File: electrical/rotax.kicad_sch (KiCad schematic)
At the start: 23 parts

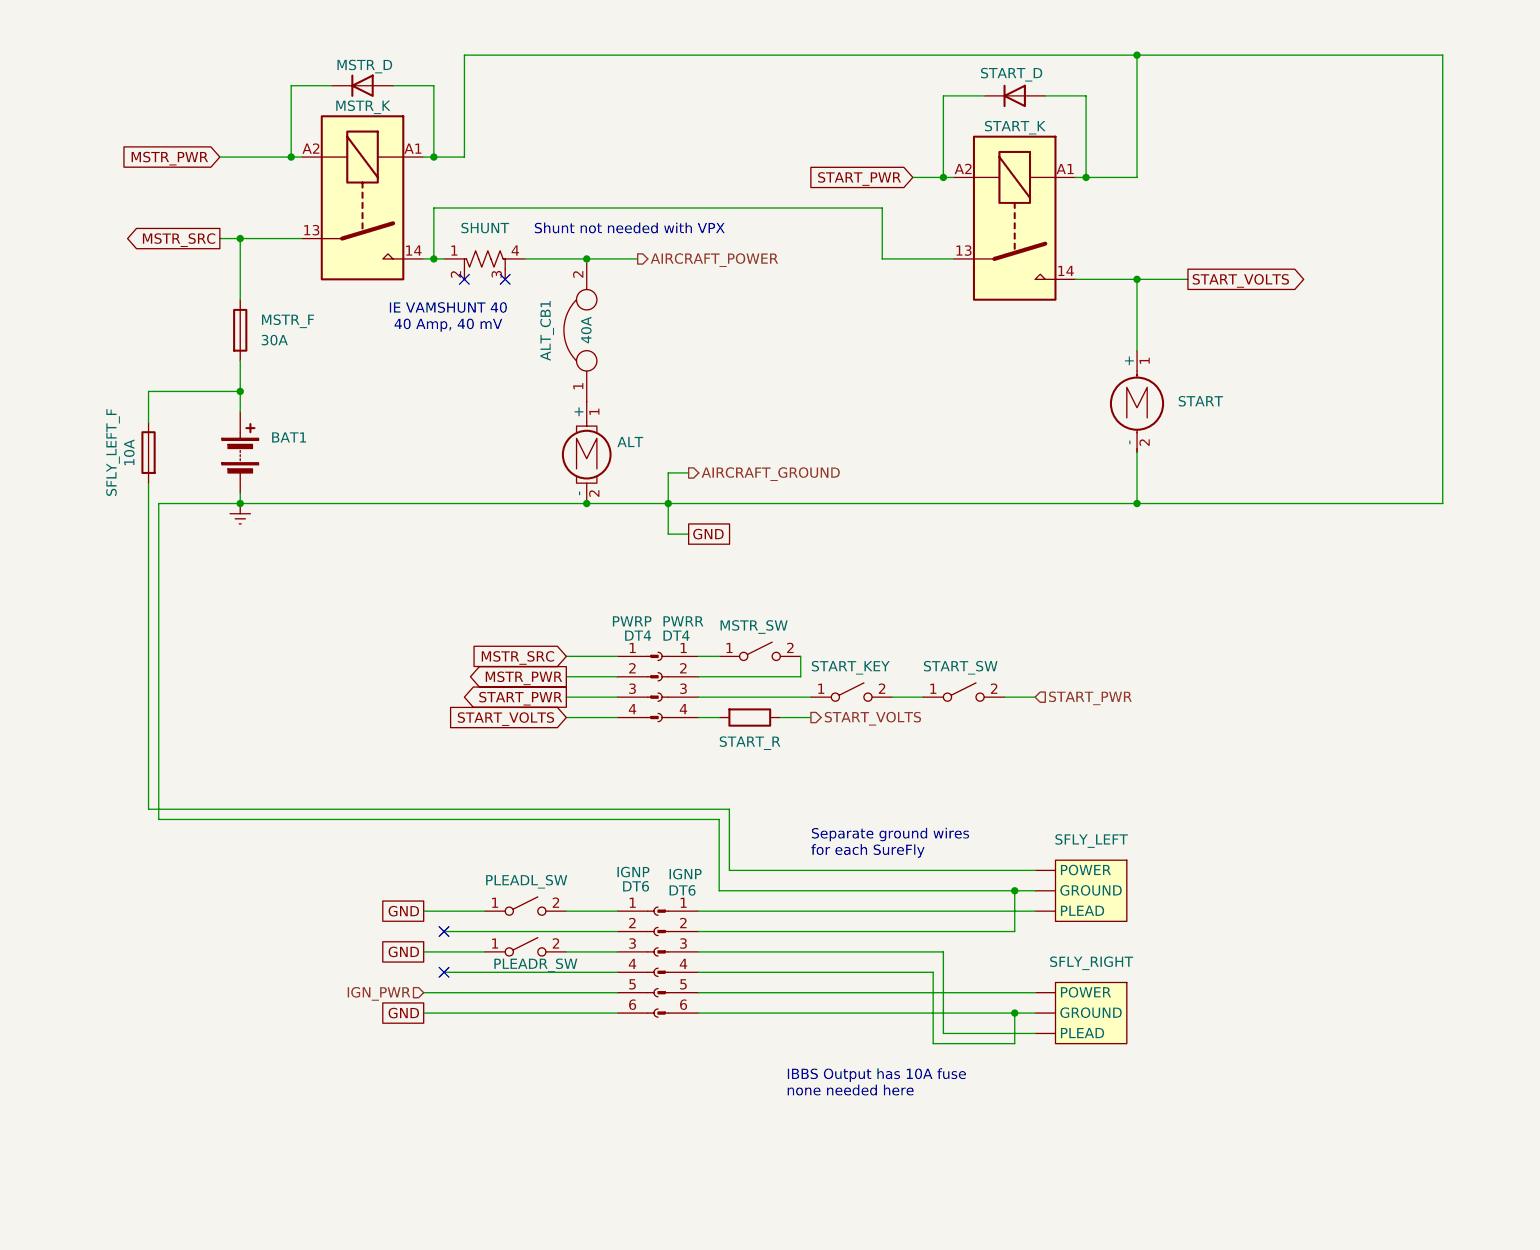
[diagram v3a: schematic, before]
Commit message: Added amperage and gauges for wires.
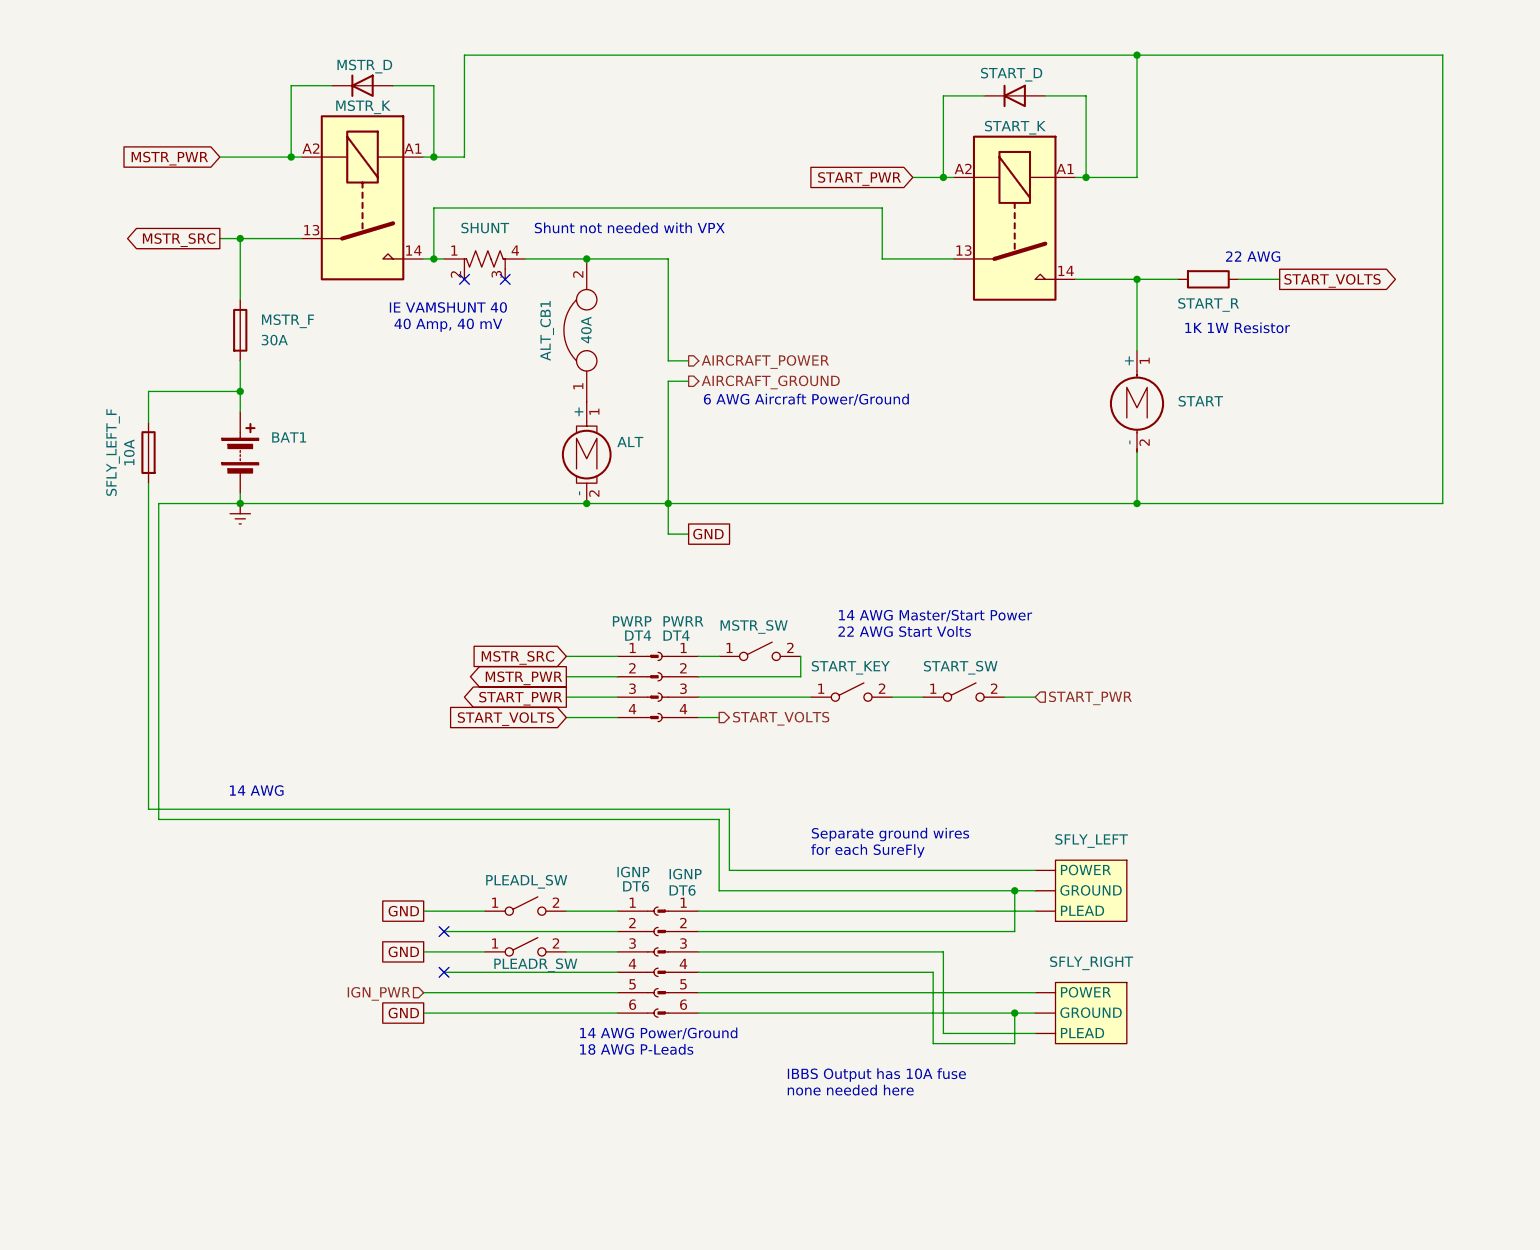
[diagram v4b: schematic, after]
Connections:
- net START_VOLTS: now also PWRR.4 (Pin_4); no longer START.1 (+), START_K.14
- net at START_R.2: now also START.1 (+), START_K.14; no longer PWRR.4 (Pin_4)
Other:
- note added: "14 AWG"
- note added: "14 AWG Master/Start Power 22 AWG Start Volts"
- note added: "14 AWG Power/Ground 18 AWG P-Leads"
- note added: "1K 1W Resistor"
- note added: "22 AWG"
- note added: "6 AWG Aircraft Power/Ground"
- moved on the sheet: START_R
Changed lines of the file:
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@@
 		(title "Lycoming")
 		(date "2025-10-01")
-		(rev "1.1")
+		(rev "1.1.1")
 		(company "N78HR")
 	)
@@
 		)
 	)
+	(text "1K 1W Resistor"
+		(exclude_from_sim no)
+		(at 167.386 53.34 0)
+		(effects
+			(font
+				(size 1.27 1.27)
+			)
+		)
+	)
 	(text "Separate ground wires\nfor each SureFly"
 		(exclude_from_sim no)
@@
 		)
 	)
+	(text "14 AWG Power/Ground\n18 AWG P-Leads"
+		(exclude_from_sim no)
+		(at 85.344 142.24 0)
+		(effects
+			(font
+				(size 1.27 1.27)
+			)
+			(justify left)
+		)
+	)
 	(text "IBBS Output has 10A fuse\nnone needed here"
 		(exclude_from_sim no)
@@
 		)
 	)
+	(text "6 AWG Aircraft Power/Ground"
+		(exclude_from_sim no)
+		(at 100.838 62.23 0)
+		(effects
+			(font
+				(size 1.27 1.27)
+			)
+			(justify left)
+		)
+	)
+	(text "14 AWG Master/Start Power\n22 AWG Start Volts"
+		(exclude_from_sim no)
+		(at 117.602 90.17 0)
+		(effects
+			(font
+				(size 1.27 1.27)
+			)
+			(justify left)
+		)
+	)
 	(text "IE VAMSHUNT 40\n40 Amp, 40 mV"
 		(exclude_from_sim no)
 		(at 69.088 51.816 0)
+		(effects
+			(font
+				(size 1.27 1.27)
+			)
+		)
+	)
+	(text "14 AWG"
+		(exclude_from_sim no)
+		(at 45.212 110.998 0)
+		(effects
+			(font
+				(size 1.27 1.27)
+			)
+		)
+	)
+	(text "22 AWG"
+		(exclude_from_sim no)
+		(at 169.418 44.45 0)
 		(effects
 			(font
@@
 	)
 	(junction
-		(at 154.94 46.99)
-		(diameter 0)
-		(color 0 0 0 0)
-	)
-	(junction
 		(at 96.52 74.93)
 		(diameter 0)
@@
 	)
 	(junction
+		(at 154.94 46.99)
+		(diameter 0)
+		(color 0 0 0 0)
+	)
+	(junction
 		(at 148.59 34.29)
 		(diameter 0)
@@
 	(wire
 		(pts
+			(xy 100.33 101.6) (xy 102.87 101.6)
+		)
+		(stroke
+			(width 0)
+			(type default)
+		)
+	)
+	(wire
+		(pts
 			(xy 100.33 99.06) (xy 114.3 99.06)
 		)
@@
 	(wire
 		(pts
-			(xy 92.71 44.45) (xy 86.36 44.45)
+			(xy 99.06 57.15) (xy 96.52 57.15)
 		)
 		(stroke
@@
 	(wire
 		(pts
-			(xy 100.33 101.6) (xy 102.87 101.6)
-		)
-		(stroke
-			(width 0)
-			(type default)
-		)
-	)
-	(wire
-		(pts
 			(xy 100.33 135.89) (xy 142.24 135.89)
 		)
@@
 	(wire
 		(pts
-			(xy 154.94 46.99) (xy 161.29 46.99)
-		)
-		(stroke
-			(width 0)
-			(type default)
-		)
-	)
-	(wire
-		(pts
 			(xy 68.58 128.27) (xy 90.17 128.27)
 		)
@@
 	(wire
 		(pts
-			(xy 110.49 101.6) (xy 114.3 101.6)
-		)
-		(stroke
-			(width 0)
-			(type default)
-		)
-	)
-	(wire
-		(pts
 			(xy 31.75 72.39) (xy 31.75 113.03)
 		)
@@
 	(wire
 		(pts
+			(xy 96.52 57.15) (xy 96.52 44.45)
+		)
+		(stroke
+			(width 0)
+			(type default)
+		)
+	)
+	(wire
+		(pts
 			(xy 71.12 19.05) (xy 154.94 19.05)
 		)
@@
 	(wire
 		(pts
-			(xy 99.06 71.12) (xy 96.52 71.12)
+			(xy 99.06 59.69) (xy 96.52 59.69)
 		)
 		(stroke
@@
 	(wire
 		(pts
+			(xy 167.64 46.99) (xy 172.72 46.99)
+		)
+		(stroke
+			(width 0)
+			(type default)
+		)
+	)
+	(wire
+		(pts
 			(xy 100.33 138.43) (xy 139.7 138.43)
 		)
@@
 	(wire
 		(pts
+			(xy 154.94 46.99) (xy 160.02 46.99)
+		)
+		(stroke
+			(width 0)
+			(type default)
+		)
+	)
+	(wire
+		(pts
+			(xy 96.52 44.45) (xy 86.36 44.45)
+		)
+		(stroke
+			(width 0)
+			(type default)
+		)
+	)
+	(wire
+		(pts
 			(xy 143.51 24.13) (xy 148.59 24.13)
 		)
@@
 	(wire
 		(pts
-			(xy 96.52 71.12) (xy 96.52 74.93)
+			(xy 96.52 59.69) (xy 96.52 74.93)
 		)
 		(stroke
@@
 	(global_label "START_VOLTS"
 		(shape output)
-		(at 161.29 46.99 0)
+		(at 172.72 46.99 0)
 		(fields_autoplaced yes)
 		(effects
@@
 		)
 		(property "Intersheetrefs" "${INTERSHEET_REFS}"
-			(at 176.3704 46.99 0)
+			(at 187.8004 46.99 0)
 			(effects
 				(font
@@
 	(hierarchical_label "START_VOLTS"
 		(shape output)
-		(at 114.3 101.6 0)
+		(at 102.87 101.6 0)
 		(effects
 			(font
@@
 	(hierarchical_label "AIRCRAFT_POWER"
 		(shape output)
-		(at 92.71 44.45 0)
+		(at 99.06 57.15 0)
 		(effects
 			(font
@@
 	(hierarchical_label "AIRCRAFT_GROUND"
 		(shape output)
-		(at 99.06 71.12 0)
+		(at 99.06 59.69 0)
 		(effects
 			(font
@@
 	(symbol
 		(lib_id "Device:R")
-		(at 106.68 101.6 270)
+		(at 163.83 46.99 270)
 		(unit 1)
 		(exclude_from_sim no)
@@
 		(dnp no)
 		(property "Reference" "START_R"
-			(at 106.68 104.648 90)
+			(at 163.83 50.038 90)
 			(effects
 				(font
@@
 		)
 		(property "Value" "R"
-			(at 105.4101 104.14 0)
+			(at 162.5601 49.53 0)
 			(effects
 				(font
@@
 		)
 		(property "Footprint" ""
-			(at 106.68 99.822 90)
+			(at 163.83 45.212 90)
 			(effects
 				(font
@@
 		)
 		(property "Datasheet" "~"
-			(at 106.68 101.6 0)
+			(at 163.83 46.99 0)
 			(effects
 				(font
@@
 		)
 		(property "Description" "Resistor"
-			(at 106.68 101.6 0)
-			(effects
-				(font
+			(at 163.83 46.99 0)
+			(effects
+				(font

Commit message: Added switch numbers.
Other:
- note added: "RS1"
- note added: "RS2"
- note added: "RS3"
- note added: "RS4"
- note added: "RS5"
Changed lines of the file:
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@@
 	(title_block
 		(title "Lycoming")
-		(date "2025-10-01")
-		(rev "1.1.1")
+		(date "2025-10-02")
+		(rev "1.1.3")
 		(company "N78HR")
 	)
@@
 		)
 	)
+	(text "RS5"
+		(exclude_from_sim no)
+		(at 71.882 124.46 0)
+		(effects
+			(font
+				(size 1.27 1.27)
+			)
+		)
+	)
 	(text "IBBS Output has 10A fuse\nnone needed here"
 		(exclude_from_sim no)
@@
 		)
 	)
+	(text "RS4"
+		(exclude_from_sim no)
+		(at 71.628 132.334 0)
+		(effects
+			(font
+				(size 1.27 1.27)
+			)
+		)
+	)
 	(text "14 AWG Master/Start Power\n22 AWG Start Volts"
 		(exclude_from_sim no)
@@
 			)
 			(justify left)
+		)
+	)
+	(text "RS2"
+		(exclude_from_sim no)
+		(at 133.096 101.854 0)
+		(effects
+			(font
+				(size 1.27 1.27)
+			)
 		)
 	)
@@
 		)
 	)
+	(text "RS3"
+		(exclude_from_sim no)
+		(at 108.204 88.138 0)
+		(effects
+			(font
+				(size 1.27 1.27)
+			)
+		)
+	)
 	(text "22 AWG"
 		(exclude_from_sim no)
@@
 		(effects
 			(font
+				(size 1.27 1.27)
+			)
+		)
+	)
+	(text "RS1"
+		(exclude_from_sim no)
+		(at 121.666 101.6 0)
+		(effects
+			(font

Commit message: Changed wiring of plead connector
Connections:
- net Earth: now also IGNP.4 (Pin_4); no longer IGNP.6 (Pin_6)
- net IGN_PWR: now also IGNP.3 (Pin_3); no longer IGNP.5 (Pin_5)
- net at IGNP.6 (Pin_6), SFLY_RIGHT. (PLEAD): no longer IGNP.4 (Pin_4)
- net at IGNP.5 (Pin_5), SFLY_RIGHT. (PLEAD): now also IGNP.4 (Pin_4)
- net at PLEADR_SW.2 (B): now also IGNP.6 (Pin_6); no longer IGNP.3 (Pin_3)
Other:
- moved on the sheet: PLEADR_SW, SFLY_RIGHT
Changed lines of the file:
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@@
 	(title_block
 		(title "Lycoming")
-		(date "2025-10-02")
-		(rev "1.1.3")
+		(date "2025-10-11")
+		(rev "1.1.7")
 		(company "N78HR")
 	)
@@
 	(text "RS4"
 		(exclude_from_sim no)
-		(at 71.628 132.334 0)
+		(at 71.628 139.954 0)
 		(effects
 			(font
@@
 	)
 	(junction
+		(at 138.43 133.35)
+		(diameter 0)
+		(color 0 0 0 0)
+	)
+	(junction
 		(at 96.52 74.93)
 		(diameter 0)
@@
 	)
 	(junction
-		(at 139.7 138.43)
-		(diameter 0)
-		(color 0 0 0 0)
-	)
-	(junction
 		(at 139.7 123.19)
 		(diameter 0)
@@
 	)
 	(no_connect
-		(at 68.58 133.35)
+		(at 68.58 135.89)
 	)
 	(wire
@@
 	(wire
 		(pts
+			(xy 68.58 135.89) (xy 90.17 135.89)
+		)
+		(stroke
+			(width 0)
+			(type default)
+		)
+	)
+	(wire
+		(pts
 			(xy 100.33 99.06) (xy 114.3 99.06)
 		)
@@
 	(wire
 		(pts
-			(xy 130.81 130.81) (xy 130.81 140.97)
-		)
-		(stroke
-			(width 0)
-			(type default)
-		)
-	)
-	(wire
-		(pts
 			(xy 100.33 93.98) (xy 102.87 93.98)
 		)
@@
 	(wire
 		(pts
-			(xy 66.04 138.43) (xy 90.17 138.43)
+			(xy 140.97 135.89) (xy 140.97 138.43)
 		)
 		(stroke
@@
 	(wire
 		(pts
-			(xy 66.04 130.81) (xy 73.66 130.81)
+			(xy 66.04 138.43) (xy 73.66 138.43)
 		)
 		(stroke
@@
 	(wire
 		(pts
+			(xy 140.97 135.89) (xy 142.24 135.89)
+		)
+		(stroke
+			(width 0)
+			(type default)
+		)
+	)
+	(wire
+		(pts
 			(xy 100.33 125.73) (xy 142.24 125.73)
 		)
@@
 	(wire
 		(pts
-			(xy 100.33 135.89) (xy 142.24 135.89)
-		)
-		(stroke
-			(width 0)
-			(type default)
-		)
-	)
-	(wire
-		(pts
 			(xy 40.64 41.91) (xy 43.18 41.91)
 		)
@@
 	(wire
 		(pts
-			(xy 139.7 142.24) (xy 139.7 138.43)
-		)
-		(stroke
-			(width 0)
-			(type default)
-		)
-	)
-	(wire
-		(pts
 			(xy 49.53 31.75) (xy 50.8 31.75)
 		)
@@
 	(wire
 		(pts
-			(xy 83.82 130.81) (xy 90.17 130.81)
-		)
-		(stroke
-			(width 0)
-			(type default)
-		)
-	)
-	(wire
-		(pts
 			(xy 67.31 44.45) (xy 68.58 44.45)
 		)
@@
 	(wire
 		(pts
+			(xy 100.33 130.81) (xy 142.24 130.81)
+		)
+		(stroke
+			(width 0)
+			(type default)
+		)
+	)
+	(wire
+		(pts
 			(xy 193.04 19.05) (xy 193.04 74.93)
 		)
@@
 	(wire
 		(pts
-			(xy 139.7 138.43) (xy 142.24 138.43)
-		)
-		(stroke
-			(width 0)
-			(type default)
-		)
-	)
-	(wire
-		(pts
 			(xy 130.81 24.13) (xy 130.81 34.29)
 		)
@@
 	(wire
 		(pts
+			(xy 100.33 133.35) (xy 138.43 133.35)
+		)
+		(stroke
+			(width 0)
+			(type default)
+		)
+	)
+	(wire
+		(pts
 			(xy 68.58 128.27) (xy 90.17 128.27)
 		)
@@
 	(wire
 		(pts
-			(xy 130.81 140.97) (xy 142.24 140.97)
-		)
-		(stroke
-			(width 0)
-			(type default)
-		)
-	)
-	(wire
-		(pts
-			(xy 100.33 130.81) (xy 130.81 130.81)
+			(xy 100.33 135.89) (xy 138.43 135.89)
+		)
+		(stroke
+			(width 0)
+			(type dash)
+		)
+	)
+	(wire
+		(pts
+			(xy 66.04 130.81) (xy 90.17 130.81)
 		)
 		(stroke
@@
 	(wire
 		(pts
-			(xy 66.04 135.89) (xy 90.17 135.89)
+			(xy 83.82 138.43) (xy 90.17 138.43)
+		)
+		(stroke
+			(width 0)
+			(type default)
+		)
+	)
+	(wire
+		(pts
+			(xy 138.43 133.35) (xy 138.43 135.89)
 		)
 		(stroke
@@
 	(wire
 		(pts
-			(xy 68.58 133.35) (xy 90.17 133.35)
-		)
-		(stroke
-			(width 0)
-			(type dash)
-		)
-	)
-	(wire
-		(pts
 			(xy 154.94 55.88) (xy 154.94 46.99)
 		)
@@
 	(wire
 		(pts
-			(xy 100.33 133.35) (xy 129.54 133.35)
-		)
-		(stroke
-			(width 0)
-			(type dash)
+			(xy 66.04 133.35) (xy 90.17 133.35)
+		)
+		(stroke
+			(width 0)
+			(type default)
 		)
 	)
@@
 	(wire
 		(pts
-			(xy 100.33 138.43) (xy 139.7 138.43)
-		)
-		(stroke
-			(width 0)
-			(type default)
-		)
-	)
-	(wire
-		(pts
-			(xy 129.54 133.35) (xy 129.54 142.24)
-		)
-		(stroke
-			(width 0)
-			(type dash)
+			(xy 140.97 138.43) (xy 100.33 138.43)
+		)
+		(stroke
+			(width 0)
+			(type default)
 		)
 	)
@@
 	(wire
 		(pts
+			(xy 138.43 133.35) (xy 142.24 133.35)
+		)
+		(stroke
+			(width 0)
+			(type default)
+		)
+	)
+	(wire
+		(pts
 			(xy 147.32 34.29) (xy 148.59 34.29)
 		)
@@
 			(width 0)
 			(type default)
-		)
-	)
-	(wire
-		(pts
-			(xy 129.54 142.24) (xy 139.7 142.24)
-		)
-		(stroke
-			(width 0)
-			(type dash)
 		)
 	)
@@
 	(global_label "GND"
 		(shape passive)
-		(at 66.04 130.81 180)
+		(at 66.04 138.43 180)
 		(fields_autoplaced yes)
 		(effects
@@
 		)
 		(property "Intersheetrefs" "${INTERSHEET_REFS}"
-			(at 60.2956 130.81 0)
+			(at 60.2956 138.43 0)
 			(effects
 				(font
@@
 	(global_label "GND"
 		(shape passive)
-		(at 66.04 138.43 180)
+		(at 66.04 133.35 180)
 		(fields_autoplaced yes)
 		(effects
@@
 		)
 		(property "Intersheetrefs" "${INTERSHEET_REFS}"
-			(at 60.2956 138.43 0)
+			(at 60.2956 133.35 0)
 			(effects
 				(font
@@
 	(hierarchical_label "IGN_PWR"
 		(shape input)
-		(at 66.04 135.89 180)
+		(at 66.04 130.81 180)
 		(effects
 			(font
@@
 	(symbol
 		(lib_id "Switch:SW_SPST")
-		(at 78.74 130.81 0)
+		(at 78.74 138.43 0)
 		(unit 1)
 		(exclude_from_sim no)
@@
 		(dnp no)
 		(property "Reference" "PLEADR_SW"
-			(at 74.676 132.334 0)
+			(at 74.676 139.954 0)
 			(effects
 				(font
@@
 		)
 		(property "Value" "~"
-			(at 78.74 127 0)
+			(at 78.74 134.62 0)
 			(effects
 				(font
@@
 		)
 		(property "Footprint" ""
-			(at 78.74 130.81 0)
+			(at 78.74 138.43 0)
 			(effects
 				(font
@@
 		)
 		(property "Datasheet" "~"
-			(at 78.74 130.81 0)
+			(at 78.74 138.43 0)
 			(effects
 				(font
@@
 		)
 		(property "Description" ""
-			(at 78.74 130.81 0)
+			(at 78.74 138.43 0)
 			(effects
 				(font
@@
 		(lib_name "SureFly_SIM_1")
 		(lib_id "flyerx:SureFly_SIM")
-		(at 153.67 134.62 0)
+		(at 153.67 129.54 0)
 		(mirror y)
 		(unit 1)
@@
 		(dnp no)
 		(property "Reference" "SFLY_RIGHT"
-			(at 149.225 132.08 0)
+			(at 149.098 139.7 0)
 			(effects
 				(font
@@
 		)
 		(property "Value" "~"
-			(at 149.225 132.08 0)
+			(at 149.225 127 0)
 			(effects
 				(font
@@
 		)
 		(property "Footprint" ""
-			(at 158.75 133.35 0)
+			(at 158.75 128.27 0)
 			(effects
 				(font
@@
 		)
 		(property "Datasheet" ""
-			(at 158.75 133.35 0)
+			(at 158.75 128.27 0)
 			(effects
 				(font
@@
 		)
 		(property "Description" ""
-			(at 158.75 134.62 0)
-			(effects
-				(font
+			(at 158.75 129.54 0)
+			(effects
+				(font

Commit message: Added Field Wire and Alternator symbol.
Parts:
- removed ALT: Motor_DC_ALT, symbol Motor:Motor_DC_ALT
- added A1: Alternator_Regulated, symbol flyerx:Alternator_Regulated
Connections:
- net Earth: now also A1.G
- net at ALT_CB1.1: now also A1.B
- new net ALT_ON: A1.IG
- no-connect marks 4 -> 5
